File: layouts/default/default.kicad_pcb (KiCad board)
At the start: 2 copper layers, 104 x 36 mm, 73 parts

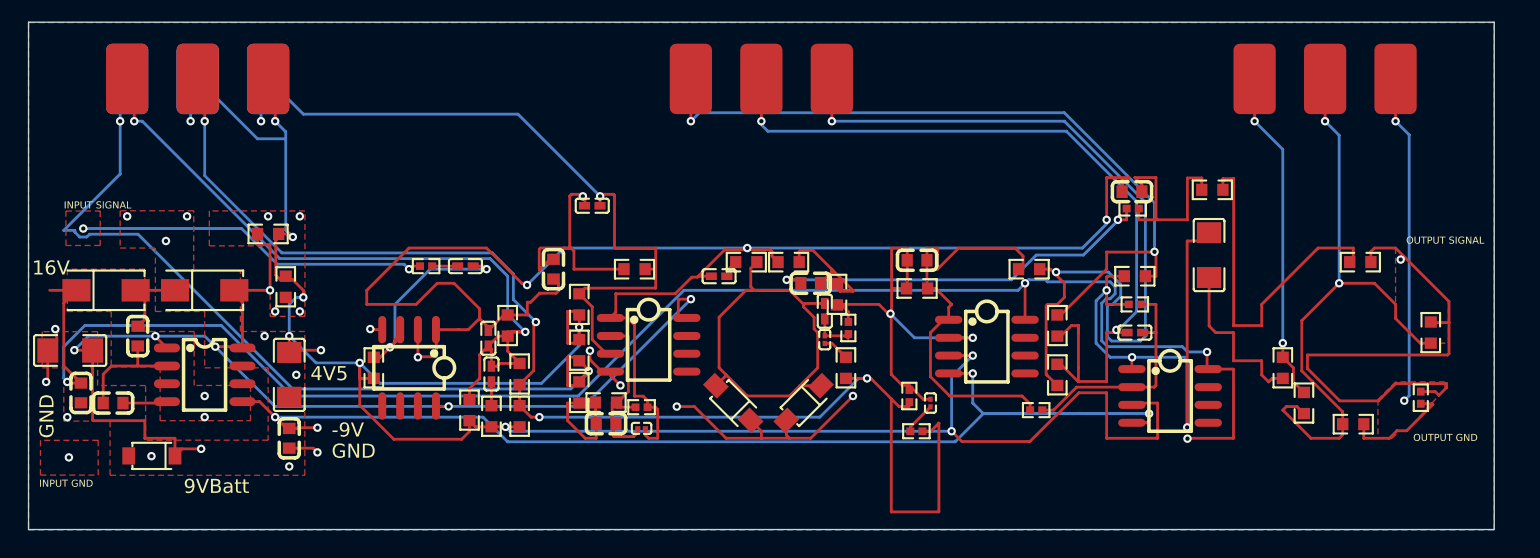
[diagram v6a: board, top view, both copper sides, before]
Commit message: update layout with test pads
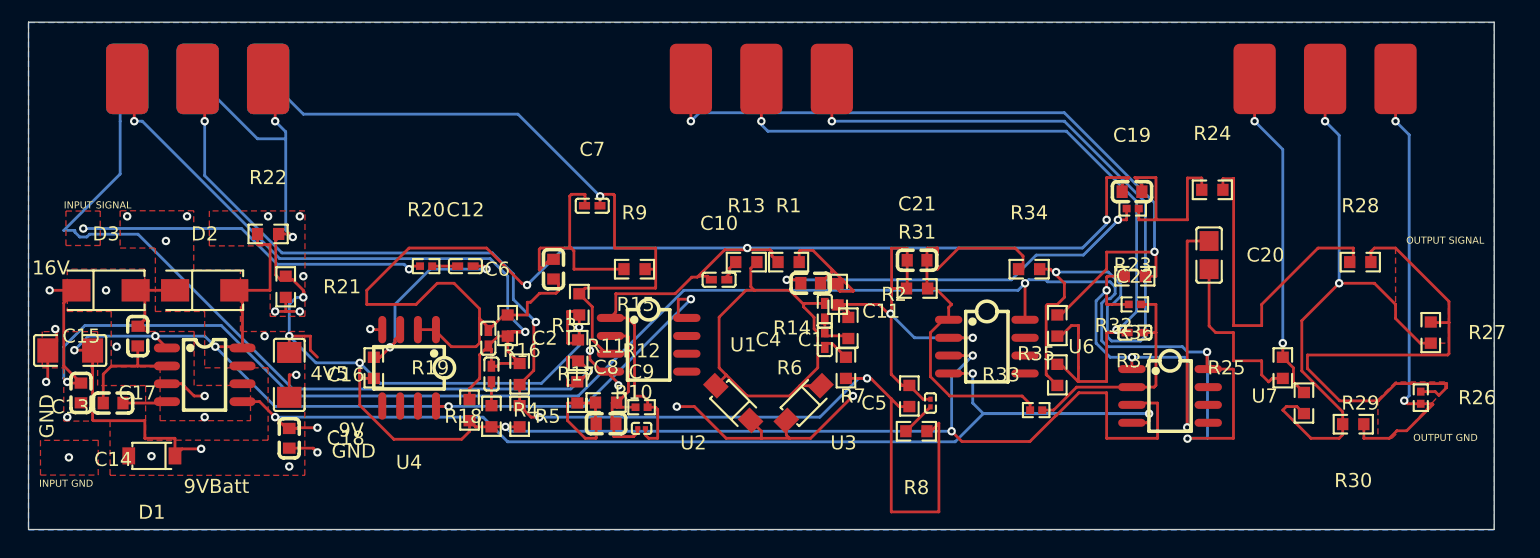
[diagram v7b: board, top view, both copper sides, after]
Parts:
- C13, C16: footprint Murata_Electronics_GRM31CR61E476ME44L:C1206 -> TDK_C3216X5R1E476MTJ00E:C1206
- C2, C7: value 68nF ±10% 16V X7R -> 68nF ±5% 16V X7R; footprint YAGEO_CC0402KRX7R7BB683:C0402 -> YAGEO_CC0402JRX7R7BB683:C0402
- C20: value 4.7µF ±10% 50V X7R -> 4.7µF ±10% 50V X5R; footprint FH_1206B475K500NT:C1206 -> Samsung_Electro_Mechanics_CL21A475KBQNNNE:C0805
- C22: footprint FH_0402B392K500NT:C0402 -> Darfon_Elec_C1005X7R392KGTS:C0402
- C4: value 2.2nF ±10% 25V X7R -> 2.2nF ±10% 16V X7R; footprint Murata_Electronics_GRM033R71E222KA12D:C0201 -> YAGEO_CC0402KRX7R7BB222:C0402
- R14: value 47kΩ ±1% 62.5mW -> 47kΩ ±1% 100mW; footprint UNI_ROYAL_0402WGF4702TCE:R0402 -> FOJAN_FRC0603F4702TS:R0603
- R7: value 27kΩ ±1% 62.5mW -> 27kΩ ±1% 100mW; footprint UNI_ROYAL_0402WGF2702TCE:R0402 -> UNI_ROYAL_0603WAF2702T5E:R0603
- R8: value 12kΩ ±1% 62.5mW -> 12kΩ ±1% 100mW; footprint RALEC_RTT021202FTH:R0402 -> UNI_ROYAL_0603WAF1202T5E:R0603
- moved C10 0.25 mm to (117.0, 82.2)
- moved R10 0.14 mm to (106.9, 90.2)
- moved R16 0.08 mm to (107.0, 87.3)
- moved R2 0.05 mm to (125.4, 83.3)
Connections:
- net INPUT renamed -INPUT-0
- net INPUT-1 renamed -INPUT-1
- net P1INminus renamed -P1INminus
- net gain_stage-net renamed gain_stage-net-0
- net gain_stage-tap renamed gain_stage-tap-0
- net gnd renamed -gnd-0
- net gnd-1 renamed -gnd-1
- net gnd-2 renamed -gnd-2
- net gnd-3 renamed -gnd-3
- net hv renamed -hv-0
- net hv-1 renamed -hv-1
- net hv-2 renamed -hv-2
- net line renamed -line
- net output renamed -output-0
- net output-1 renamed -output-1
- net output-2 renamed -output-2
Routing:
- net -gnd-0: track 28.4 -> 36.3 mm, vias 23 -> 26
- net -hv-2: track 120.1 -> 127.6 mm, vias 4 -> 5
- net gain_stage-P1INplus: track 53.4 -> 50.9 mm, vias 2 -> 1
- net -output-0: track 121.3 -> 119.3 mm, vias 4 -> 3
- net -hv-1: track 149.5 -> 148.1 mm, vias 11 -> 9
- net -gnd-2: track 31.2 -> 32.4 mm
- net gain_stage-resistors_ifs[1]: vias 2 -> 1
- net gain_stage-net-3: vias 1 -> 0
- net -hv-0: vias 7 -> 6
- net -INPUT-1: vias 1 -> 0
